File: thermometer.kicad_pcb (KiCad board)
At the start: 2 copper layers, 68.4 x 36.7 mm, 34 parts, among them IC1 ATTINY2313A-P, P1 CONN_4, P2 CONN_4, P3 CONN_6, P4 CONN_4, P5 CONN_4

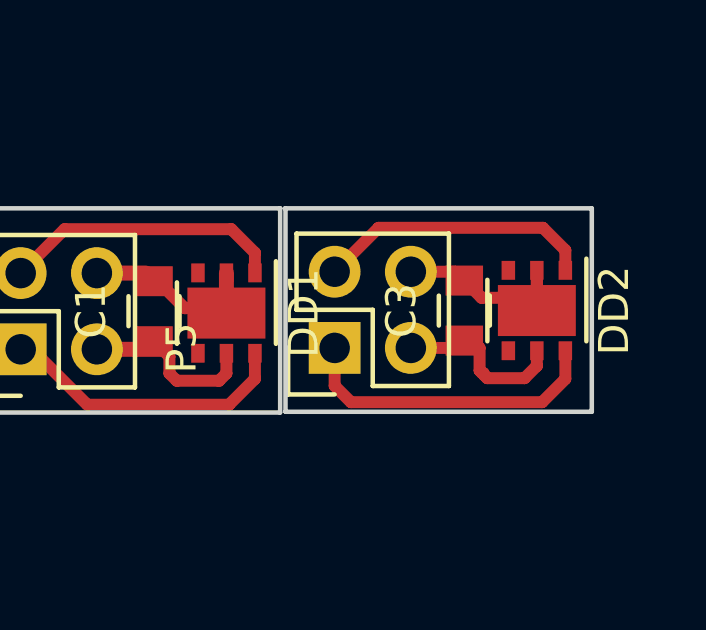
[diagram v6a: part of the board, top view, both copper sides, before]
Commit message: Add Makefile
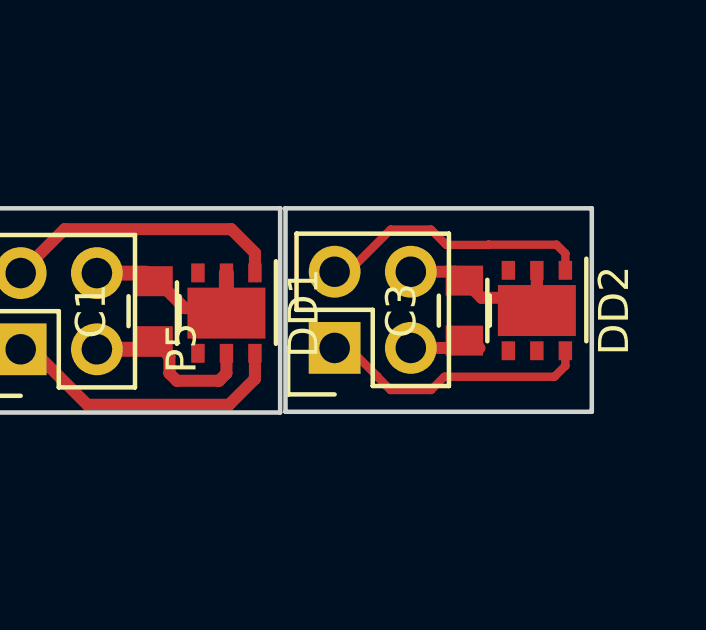
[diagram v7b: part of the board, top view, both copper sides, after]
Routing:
- net VCC: track 12.0 -> 8.62 mm
- net Net-(DD2-Pad6): track 10.3 -> 9.07 mm
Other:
- net class Default: clearance 0.4 -> 0.3; trace_width 0.4 -> 0.28
- rule trace_clearance: 0.4 -> 0.3
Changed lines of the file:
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@@
     (links 98)
     (no_connects 6)
-    (area 122.098999 79.884199 190.600401 116.711801)
+    (area 118.56574 76.4265 192.56132 120.667133)
     (thickness 1.6)
     (drawings 15)
-    (tracks 335)
+    (tracks 337)
     (zones 0)
     (modules 34)
@@
   )
   (setup
-    (last_trace_width 0.4)
-    (trace_clearance 0.4)
+    (last_trace_width 0.28)
+    (trace_clearance 0.3)
     (zone_clearance 0.508)
     (zone_45_only no)
@@
   (net 36 "Net-(DD2-Pad1)")
   (net_class Default "Это класс цепей по умолчанию."
-    (clearance 0.4)
-    (trace_width 0.4)
+    (clearance 0.3)
+    (trace_width 0.28)
     (via_dia 0.8)
     (via_drill 0.7)
@@
   (segment (start 147.9169 90.3859) (end 146.7866 90.3859) (width 0.5) (layer B.Cu) (net 21) (status 30))
   (segment (start 186.27598 98.69424) (end 186.5376 98.69424) (width 0.4) (layer F.Cu) (net 22))
-  (segment (start 186.918819 99.826761) (end 187.038819 99.946761) (width 0.4) (layer F.Cu) (net 22))
   (segment (start 186.5376 98.69424) (end 186.78398 98.94062) (width 0.4) (layer F.Cu) (net 22))
-  (segment (start 186.78398 98.94062) (end 186.78398 99.691922) (width 0.4) (layer F.Cu) (net 22))
-  (segment (start 186.78398 99.691922) (end 186.873418 99.78136) (width 0.4) (layer F.Cu) (net 22))
-  (segment (start 186.873418 99.78136) (end 186.918819 99.78136) (width 0.4) (layer F.Cu) (net 22))
-  (segment (start 188.284819 99.946761) (end 188.69382 99.53776) (width 0.4) (layer F.Cu) (net 22))
-  (segment (start 186.918819 99.78136) (end 186.918819 99.826761) (width 0.4) (layer F.Cu) (net 22))
-  (segment (start 187.038819 99.946761) (end 188.284819 99.946761) (width 0.4) (layer F.Cu) (net 22))
-  (segment (start 188.69382 99.53776) (end 188.69382 99.141761) (width 0.4) (layer F.Cu) (net 22))
   (segment (start 184.4929 98.93808) (end 186.03214 98.93808) (width 0.4) (layer F.Cu) (net 22))
   (segment (start 186.03214 98.93808) (end 186.27598 98.69424) (width 0.4) (layer F.Cu) (net 22))
@@
   (segment (start 136.144 87.9348) (end 136.5377 87.9348) (width 0.5) (layer B.Cu) (net 34) (status 30))
   (segment (start 136.5377 87.9348) (end 139.1666 85.3059) (width 0.5) (layer B.Cu) (net 34) (status 30))
-  (segment (start 181.9529 98.93808) (end 181.9529 100.20168) (width 0.4) (layer F.Cu) (net 35))
-  (segment (start 182.497991 100.746771) (end 188.868811 100.746771) (width 0.4) (layer F.Cu) (net 35))
-  (segment (start 181.9529 100.20168) (end 182.497991 100.746771) (width 0.4) (layer F.Cu) (net 35))
-  (segment (start 188.868811 100.746771) (end 189.64382 99.971762) (width 0.4) (layer F.Cu) (net 35))
-  (segment (start 189.64382 99.971762) (end 189.64382 99.141761) (width 0.4) (layer F.Cu) (net 35))
-  (segment (start 181.9529 96.39808) (end 183.416501 94.934479) (width 0.4) (layer F.Cu) (net 36))
-  (segment (start 183.416501 94.934479) (end 188.896541 94.934479) (width 0.4) (layer F.Cu) (net 36))
-  (segment (start 188.896541 94.934479) (end 189.64382 95.681758) (width 0.4) (layer F.Cu) (net 36))
-  (segment (start 189.64382 95.681758) (end 189.64382 96.241759) (width 0.4) (layer F.Cu) (net 36))
+  (segment (start 181.9529 98.93808) (end 182.42788 98.93808) (width 0.28) (layer F.Cu) (net 35))
+  (segment (start 182.42788 98.93808) (end 183.37569 99.88589) (width 0.28) (layer F.Cu) (net 35))
+  (segment (start 183.37569 99.88589) (end 183.37569 99.8982) (width 0.28) (layer F.Cu) (net 35))
+  (segment (start 183.37569 99.8982) (end 183.819171 100.341681) (width 0.28) (layer F.Cu) (net 35))
+  (segment (start 189.64382 99.53518) (end 189.64382 99.081761) (width 0.28) (layer F.Cu) (net 35))
+  (segment (start 183.819171 100.341681) (end 185.166629 100.341681) (width 0.28) (layer F.Cu) (net 35))
+  (segment (start 185.166629 100.341681) (end 185.61011 99.8982) (width 0.28) (layer F.Cu) (net 35))
+  (segment (start 185.61011 99.8982) (end 189.2808 99.8982) (width 0.28) (layer F.Cu) (net 35))
+  (segment (start 189.2808 99.8982) (end 189.64382 99.53518) (width 0.28) (layer F.Cu) (net 35))
+  (segment (start 181.9529 96.39808) (end 181.95798 96.393) (width 0.28) (layer F.Cu) (net 36))
+  (segment (start 181.95798 96.393) (end 182.42065 96.393) (width 0.28) (layer F.Cu) (net 36))
+  (segment (start 182.42065 96.393) (end 183.819171 94.994479) (width 0.28) (layer F.Cu) (net 36))
+  (segment (start 183.819171 94.994479) (end 185.166629 94.994479) (width 0.28) (layer F.Cu) (net 36))
+  (segment (start 185.166629 94.994479) (end 185.67615 95.504) (width 0.28) (layer F.Cu) (net 36))
+  (segment (start 189.64382 95.789758) (end 189.64382 96.301759) (width 0.28) (layer F.Cu) (net 36))
+  (segment (start 185.67615 95.504) (end 187.079578 95.504) (width 0.28) (layer F.Cu) (net 36))
+  (segment (start 187.079578 95.504) (end 187.086819 95.496759) (width 0.28) (layer F.Cu) (net 36))
+  (segment (start 187.086819 95.496759) (end 189.350821 95.496759) (width 0.28) (layer F.Cu) (net 36))
+  (segment (start 189.350821 95.496759) (end 189.64382 95.789758) (width 0.28) (layer F.Cu) (net 36))
   (zone (net 6) (net_name GNDPWR) (layer B.Cu) (hatch edge 0.508)
     (connect_pads (clearance 0.508))

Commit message: Fixes
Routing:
- net VCC: track 8.62 -> 12.4 mm
- net Net-(DD2-Pad6): track 9.07 -> 10.5 mm
- net VDD: track 67.7 -> 68.5 mm
- net Net-(DD1-Pad6): track 9.93 -> 10.6 mm
- net Net-(DP1-Pad3): track 28.7 -> 29.3 mm
- net Net-(DD2-Pad1): track 9.12 -> 9.63 mm
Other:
- outline, holes or cut-outs redrawn
